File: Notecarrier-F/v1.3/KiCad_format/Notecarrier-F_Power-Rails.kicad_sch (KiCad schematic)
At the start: 31 parts, among them U3 TPS63020DSJR, U7 MAX17225ELT+, U8 TPS62748YFPT, U9 AP2139AK-3.3TRG1

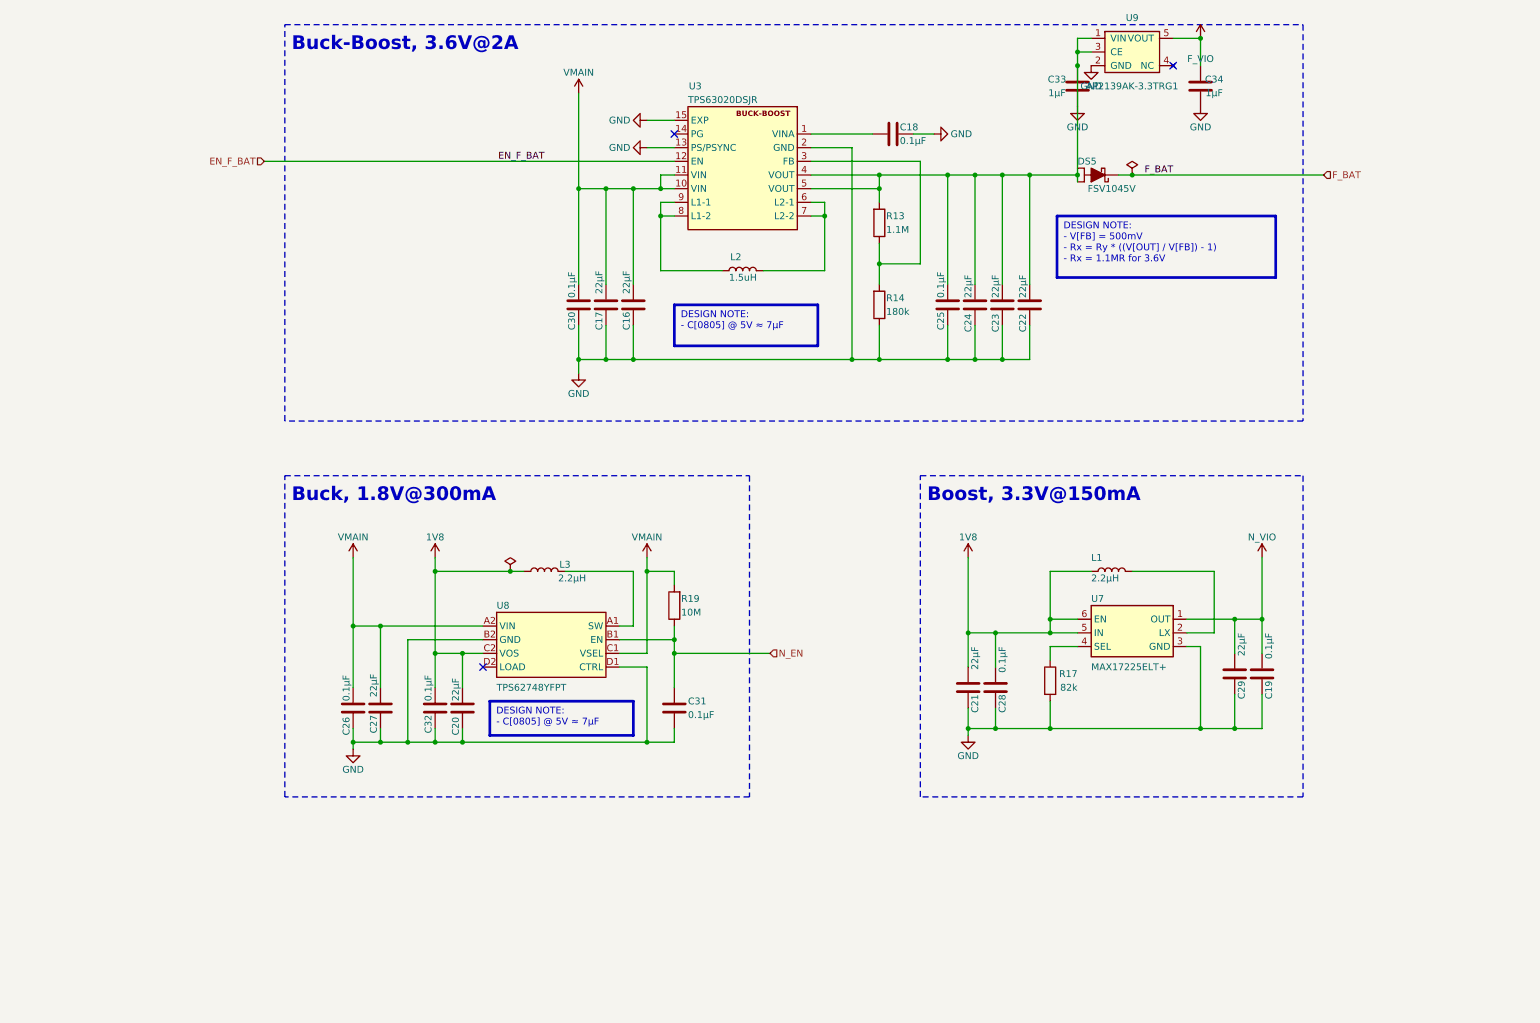
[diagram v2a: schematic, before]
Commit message: Notecarrier-F v1.3: KiCad 9 port from the release-day Altium sources
Replace the hand-made KiCad 7 port (which described v1.2, with a half-applied
v1.3 schematic delta and an ERRATA file) with a direct import of the v1.3
Altium project, recovered from the design archive's history: committed by the
design house on 2023-07-10, the day of the 2200-814 fabrication package, with a
Rev 11 schematic PDF byte-identical to the one published here. The Altium
sources are published alongside as Notecarrier-F/v1.3/Altium, as for v1.5.

The port follows the v1.5 procedure (KiCad 9.0.9 Altium project importer plus
scripted cleanup, scripts kept under documentation/scripts). All validation
gates pass: ERC 0, DRC 0 with schematic parity, BOM exact (94/94 vs
3000-653-002), placement 89/89 vs PNP-3000-653-002, gerber diff exact on outer
copper and masks with the reviewed inner-annulus/silk classes frozen as the
baseline, KiCanvas and RAG. The KiCad netlist was also matched pad by pad
against the nets carried by the Altium board file (0 conflicts).

J9/J10 are fitted per the released BOM (the 2023-08-31 re-save of the project
flips the variant to match); J11/R11/R12 are DNP. Design rules follow the
board's own Altium rule set (0.1 mm clearance). The old hand-port notes are
kept as History_Porting-Notes-hand-port.md because the harness README cites
them for the gerber-diff recipe; the RAG exclusion comment and the product
README are updated accordingly.

Co-Authored-By: Claude Fable 5.1 <noreply@anthropic.com>
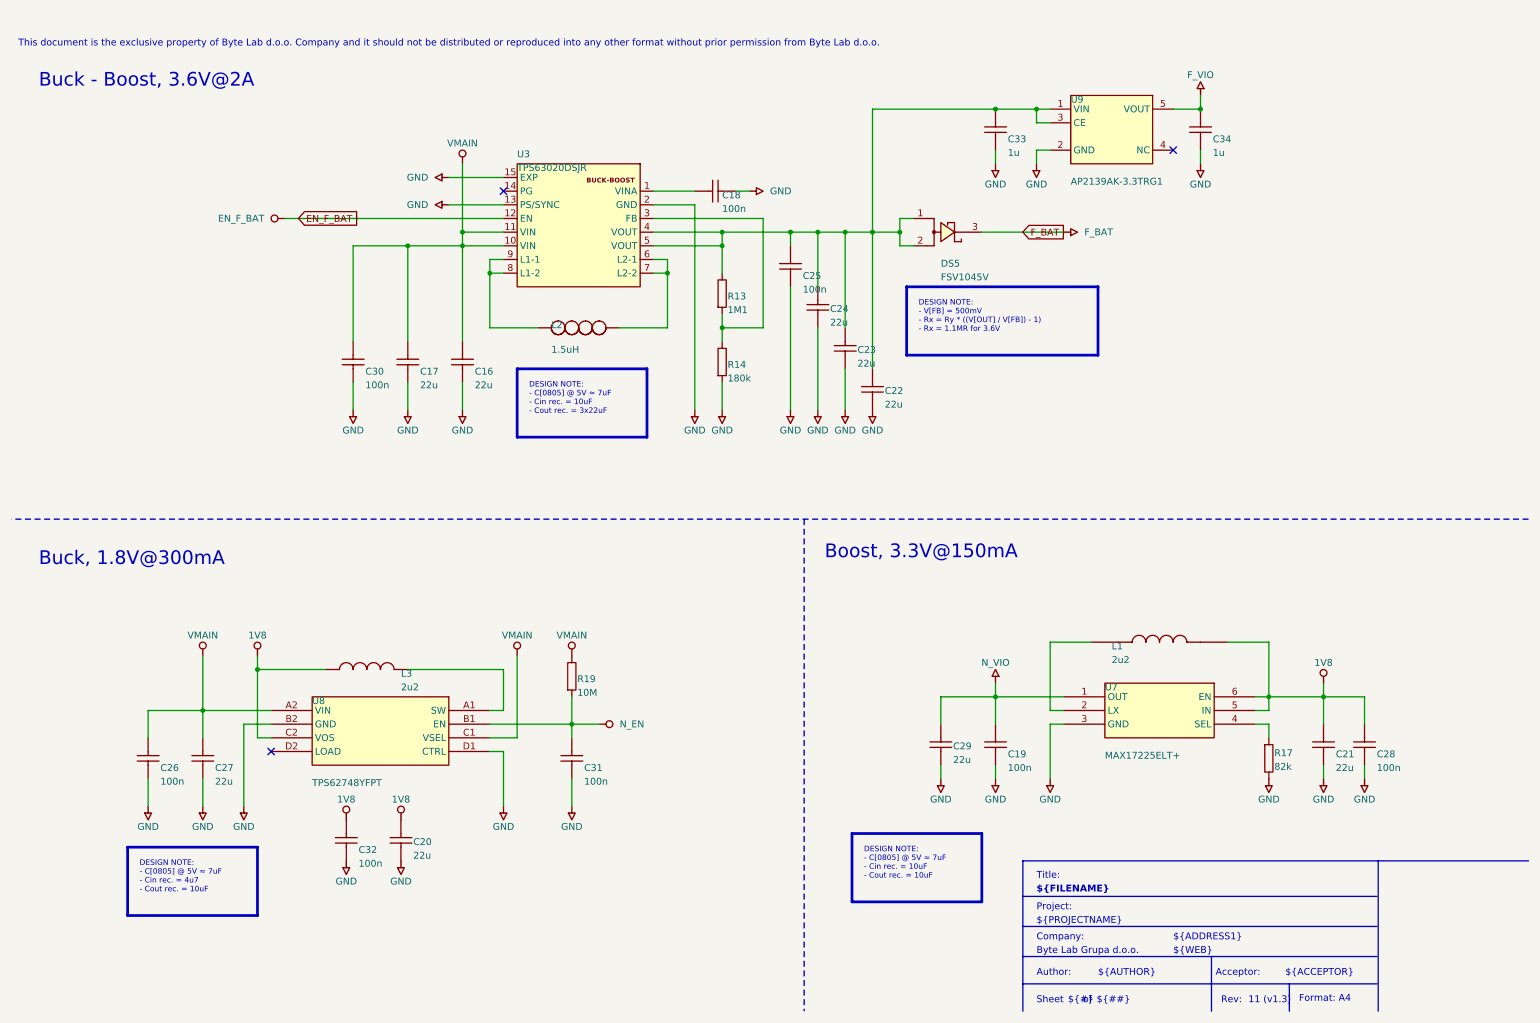
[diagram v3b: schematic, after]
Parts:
- removed C16, C17, C20, C21, C22, C23, C24, C27, C29: 22µF, blues-kicad-lib:C-0805_Fv1.2, symbol Device:C
- removed C18, C19, C25, C26, C28, C30, C31, C32: 0.1µF, blues-kicad-lib:C-0402_Fv1.2, symbol Device:C
- removed C33, C34: 1µF, blues-kicad-lib:C-0603_Fv1.2, symbol Device:C
- removed DS5: FSV1045V, blues-kicad-lib:TO277-3, symbol blues-kicad-lib:FSV1045V
- removed L1: 2.2µH, blues-kicad-lib:IND_XFL4020-222MEC_Fv1.2, symbol Device:L
- removed L2: 1.5uH, blues-kicad-lib:VCHA042A-1R5MS6_Fv1.2, symbol Device:L
- removed L3: 2.2µH, blues-kicad-lib:1285AS-H-2R2M=P2-INDC2016X100N_Fv1.2, symbol Device:L
- removed R13: 1.1M, blues-kicad-lib:R-0402_Fv1.2, symbol Device:R
- removed R14: 180k, blues-kicad-lib:R-0402_Fv1.2, symbol Device:R
- removed R17: 82k, blues-kicad-lib:R-0402_Fv1.2, symbol Device:R
- removed R19: 10M, blues-kicad-lib:R-0402_Fv1.2, symbol Device:R
- removed U3: TPS63020DSJR, blues-kicad-lib:TI PVSON-14 DSJ_Fv1.2, symbol blues-kicad-lib:TPS63020DSJR
- removed U7: MAX17225ELT+, blues-kicad-lib:MAX17225ELT+UDFN_Fv1.2, symbol blues-kicad-lib:MAX17225ELT_NoLabel
- removed U8: TPS62748YFPT, blues-kicad-lib:TPS62748YFPT-DSBGA4x2_Fv1.2, symbol blues-kicad-lib:TPS62748YFPT_NoLabel
- removed U9: AP2139AK-3.3TRG1, Notecarrier-F-local:SOT-23-5_Fv1.3, symbol Notecarrier-F-local:AP2139AK-3.3TRG1
- added C16, C17, C21, C27: 22u, Notecarrier-F-altium-import:C-0805, symbol BL_Passive:root_1_mirrored_C0805-22u-16V-X5R_BL_Passive.SchLib
- added C18: 100n, Notecarrier-F-altium-import:C-0402, symbol BL_Passive:root_0_mirrored_C0402-100n-16V-X7R_BL_Passive.SchLib
- added C19, C25, C26, C28, C30, C32: 100n, Notecarrier-F-altium-import:C-0402, symbol BL_Passive:root_1_mirrored_C0402-100n-16V-X7R_BL_Passive.SchLib
- added C20, C22, C23, C24, C29: 22u, Notecarrier-F-altium-import:C-0805, symbol BL_Passive:root_3_mirrored_C0805-22u-16V-X5R_BL_Passive.SchLib
- added C31: 100n, Notecarrier-F-altium-import:C-0402, symbol BL_Passive:root_1_C0402-100n-16V-X7R_BL_Passive.SchLib
- added C33, C34: 1u, Notecarrier-F-altium-import:C-0603, symbol BL_Passive:root_1_mirrored_C0603-1u-25V-X5R_BL_Passive.SchLib
- added DS5: FSV1045V, Notecarrier-F-altium-import:TO277-3, symbol n21-p2:root_0_SCHOTTKY - FSV1045V - 10A/45V_n21-p2.SchLib
- added L1: 2u2, Notecarrier-F-altium-import:IND_XFL4020-222MEC, symbol n21-p2:root_0_XFL4020-222MEC_n21-p2.SchLib
- added L2: 1.5uH, Notecarrier-F-altium-import:VCHA042A-1R5MS6, symbol n21-p2:root_1_mirrored_VCHA042A-1R5MS6_n21-p2.SchLib
- added L3: 2u2, Notecarrier-F-altium-import:1285AS-H-2R2M=P2-INDC2016X100N, symbol n21-p2:root_0_1285AS-H-2R2M=P2_n21-p2.SchLib
- added R13: 1M1, Notecarrier-F-altium-import:R-0402, symbol BL_Passive:root_1_mirrored_R0402-1M1-1_BL_Passive.SchLib
- added R14: 180k, Notecarrier-F-altium-import:R-0402, symbol BL_Passive:root_1_mirrored_R0402-180k-1_BL_Passive.SchLib
- added R17: 82k, Notecarrier-F-altium-import:R-0402, symbol BL_Passive:root_3_R0402-82k-1_BL_Passive.SchLib
- added R19: 10M, Notecarrier-F-altium-import:R-0402, symbol BL_Passive:root_1_mirrored_R0402-10M-1_BL_Passive.SchLib
- added U3: TPS63020DSJR, Notecarrier-F-altium-import:TI PVSON-14 DSJ, symbol n21-p2:root_0_mirrored_BUCK-BOOST - TPS63020DSJR_n21-p2.SchLib
- added U7: MAX17225ELT+, Notecarrier-F-altium-import:MAX17225ELT+UDFN, symbol n21-p2:root_0_MAX17225ELT+_n21-p2.SchLib
- added U8: TPS62748YFPT, Notecarrier-F-altium-import:TPS62748YFPT-DSBGA4x2, symbol n21-p2:root_0_TPS62748YFPT_n21-p2.SchLib
- added U9: AP2139AK-3.3TRG1, Notecarrier-F-altium-import:SOT-23-5(M5), symbol BL_Analog:root_0_AP2139AK-3.3TRG1_BL_Analog.SchLib
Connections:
- net 1V8: now also C20.1, C21.2, C28.2, C32.2, L1.2, L3.1, U7.5 (IN), U7.6 (EN), U8.C2 (VOS)
- net EN_F_BAT: now also U3.12 (EN)
- net F_BAT: now also DS5.3 (C)
- net F_VIO: now also C34.2, U9.5 (VOUT)
- net GND: now also C16.1, C17.1, C18.1, C19.1, C20.2, C21.1, C22.2, C23.2, C24.2, C25.1, C26.1, C27.1, C28.1, C29.2, C30.1, C31.1, C32.1, C33.1, C34.1, R14.1, R17.2, U3.13 (PS/SYNC), U3.15 (EXP), U3.2 (GND), U7.3 (GND), U8.B2 (GND), U8.D1 (CTRL), U9.2 (GND)
- net N_EN: now also C31.2, R19.1, U8.B1 (EN)
- net N_VIO: now also C19.2, C29.1, U7.1 (OUT)
- net VMAIN: now also C16.2, C17.2, C26.2, C27.2, C30.2, R19.2, U3.10 (VIN), U3.11 (VIN), U8.A2 (VIN), U8.C1 (VSEL)
- new net: L1.1, U7.2 (LX)
- new net: R17.1, U7.4 (SEL)
- new net: C22.1, C23.1, C24.1, C25.2, C33.2, DS5.1 (A1), DS5.2 (A2), R13.2, U3.4 (VOUT), U3.5 (VOUT), U9.1 (VIN), U9.3 (CE)
- new net: L2.1 (C), U3.6 (L2-1), U3.7 (L2-2)
- new net: L2.2 (A), U3.8 (L1-2), U3.9 (L1-1)
- new net: C18.2, U3.1 (VINA)
- new net: L3.2, U8.A1 (SW)
- new net: R13.1, R14.2, U3.3 (FB)
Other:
- note added: "${##}"
- note added: "${#}"
- note added: "${ACCEPTOR}"
- note added: "${ADDRESS1}"
- note added: "${AUTHOR}"
- note added: "${COMPANY}"
- note added: "${FILENAME}"
- note added: "${PROJECTNAME}"
- note added: "${REVISION}"
- note added: "${WEB}"
- note added: "Acceptor:"
- note added: "Author:"
- note added: "Buck - Boost, 3.6V@2A"
- note added: "Company:"
- note added: "Format: A4"
- note added: "Project:"
- note added: "Rev:"
- note added: "Sheet"
- note added: "This document is the exclusive property of Byte Lab d.o.o. Company and it should not be distributed or reproduced into any other format without prior permission from Byte Lab d.o.o."
- note added: "Title:"
- note added: "of"
- note removed: "Buck-Boost, 3.6V@2A"
- note removed: "DESIGN NOTE: - C[0805] @ 5V ≈ 7µF"
- note removed: "DESIGN NOTE: - V[FB] = 500mV - Rx = Ry * ((V[OUT] / V[FB]) - 1) - Rx = 1.1MR for 3.6V"
- company: (none) -> Byte Lab Grupa d.o.o.
